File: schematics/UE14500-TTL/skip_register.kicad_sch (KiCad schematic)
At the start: 4 parts, among them U15 74LS02, U16 74LS74

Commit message: Lay out CPU board
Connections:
- net SKIP: now reaches U16.9 (Q)
- no-connect marks 3 -> 2
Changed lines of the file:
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@@
 		(at 177.8 113.03)
 	)
-	(no_connect
-		(at 177.8 72.39)
-	)
 	(wire
 		(pts
@@
 		(pts
 			(xy 142.24 72.39) (xy 162.56 72.39)
+		)
+		(stroke
+			(width 0)
+			(type default)
+		)
+	)
+	(wire
+		(pts
+			(xy 177.8 72.39) (xy 185.42 72.39)
 		)
 		(stroke
@@
 				(hide yes)
 			)
+		)
+	)
+	(global_label "SKIP"
+		(shape output)
+		(at 185.42 72.39 0)
+		(fields_autoplaced yes)
+		(effects
+			(font
+				(size 1.27 1.27)
+			)
+			(justify left)
+		)
+		(property "Intersheetrefs" "${INTERSHEET_REFS}"
+			(at 192.7595 72.39 0)
+			(effects
+				(font
+					(size 1.27 1.27)
+				)
+				(justify left)
+				(hide yes)
+			)

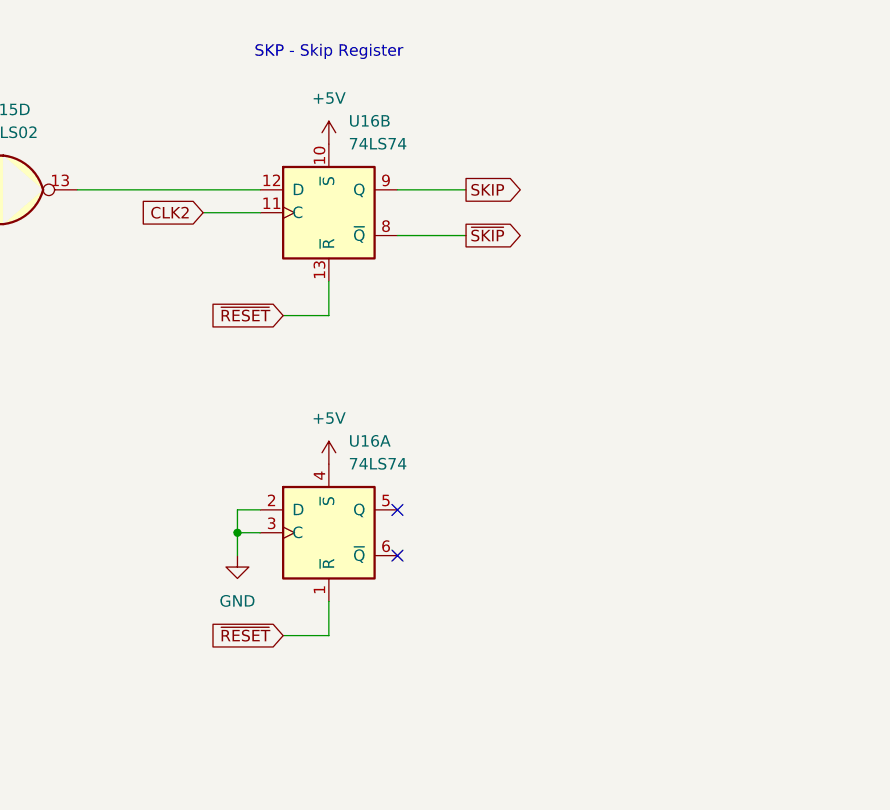
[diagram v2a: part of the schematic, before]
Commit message: Update the CPU schematic with V2 modifications
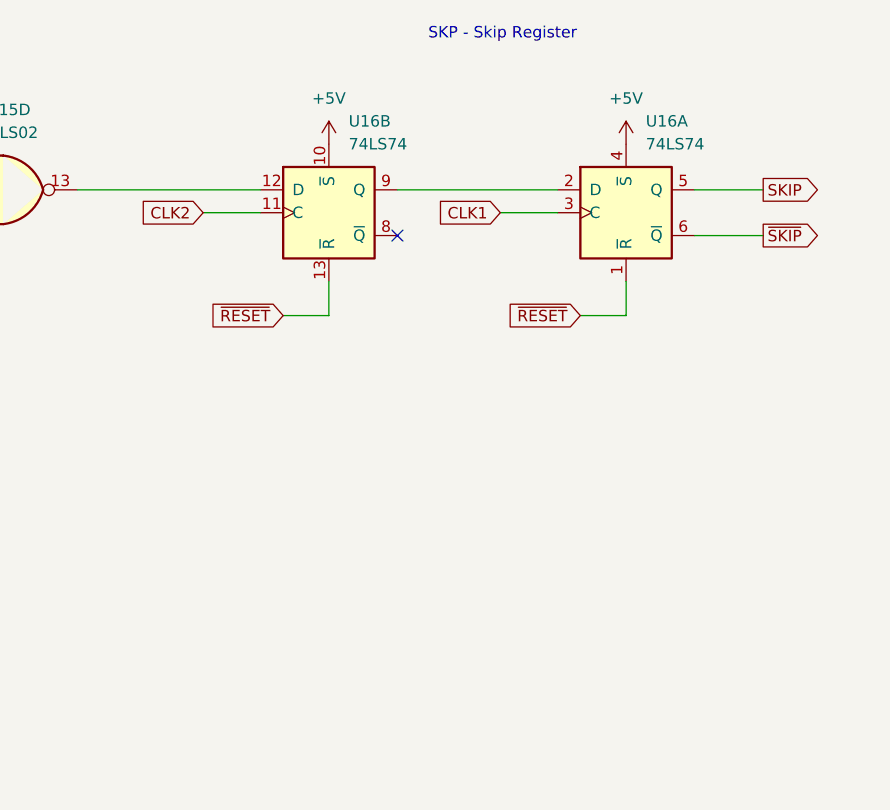
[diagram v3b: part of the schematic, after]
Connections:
- net GND: no longer U16.2 (D), U16.3 (C)
- net SKIP: now also U16.5 (Q); no longer U16.9 (Q)
- net ~{SKIP}: now also U16.6 (~{Q}); no longer U16.8 (~{Q})
- new net: U16.2 (D), U16.9 (Q)
- new net CLK1: U16.3 (C)
- no-connect marks 2 -> 1
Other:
- moved on the sheet: U16A
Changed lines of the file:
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@@
 		(title "UE14500 TTL 1-bit Microprocessor")
 		(date "2025")
-		(rev "1")
+		(rev "2")
 		(comment 1 "Copyright (c) 2025 Rhys Weatherley")
 		(comment 3 "Skip Register")
-	)
-	(junction
-		(at 160.02 110.49)
-		(diameter 0)
-		(color 0 0 0 0)
 	)
 	(junction
@@
 	)
 	(no_connect
-		(at 177.8 107.95)
-	)
-	(no_connect
-		(at 177.8 113.03)
+		(at 177.8 77.47)
 	)
 	(wire
@@
 	(wire
 		(pts
+			(xy 177.8 72.39) (xy 195.58 72.39)
+		)
+		(stroke
+			(width 0)
+			(type default)
+		)
+	)
+	(wire
+		(pts
 			(xy 156.21 74.93) (xy 162.56 74.93)
 		)
@@
 	(wire
 		(pts
-			(xy 177.8 72.39) (xy 185.42 72.39)
+			(xy 210.82 72.39) (xy 218.44 72.39)
 		)
 		(stroke
@@
 	(wire
 		(pts
-			(xy 170.18 121.92) (xy 170.18 118.11)
-		)
-		(stroke
-			(width 0)
-			(type default)
-		)
-	)
-	(wire
-		(pts
-			(xy 165.1 121.92) (xy 170.18 121.92)
+			(xy 203.2 86.36) (xy 203.2 82.55)
+		)
+		(stroke
+			(width 0)
+			(type default)
+		)
+	)
+	(wire
+		(pts
+			(xy 198.12 86.36) (xy 203.2 86.36)
 		)
 		(stroke
@@
 	(wire
 		(pts
-			(xy 160.02 110.49) (xy 160.02 107.95)
-		)
-		(stroke
-			(width 0)
-			(type default)
-		)
-	)
-	(wire
-		(pts
 			(xy 106.68 69.85) (xy 102.87 69.85)
 		)
@@
 	(wire
 		(pts
-			(xy 160.02 107.95) (xy 162.56 107.95)
-		)
-		(stroke
-			(width 0)
-			(type default)
-		)
-	)
-	(wire
-		(pts
 			(xy 80.01 66.04) (xy 80.01 60.96)
 		)
@@
 	(wire
 		(pts
-			(xy 160.02 113.03) (xy 160.02 110.49)
-		)
-		(stroke
-			(width 0)
-			(type default)
-		)
-	)
-	(wire
-		(pts
 			(xy 102.87 74.93) (xy 102.87 81.28)
 		)
@@
 	(wire
 		(pts
-			(xy 160.02 110.49) (xy 162.56 110.49)
-		)
-		(stroke
-			(width 0)
-			(type default)
-		)
-	)
-	(wire
-		(pts
 			(xy 74.93 60.96) (xy 80.01 60.96)
 		)
@@
 	(wire
 		(pts
+			(xy 189.23 74.93) (xy 195.58 74.93)
+		)
+		(stroke
+			(width 0)
+			(type default)
+		)
+	)
+	(wire
+		(pts
 			(xy 102.87 63.5) (xy 97.79 63.5)
 		)
@@
 	(wire
 		(pts
-			(xy 177.8 77.47) (xy 185.42 77.47)
+			(xy 210.82 77.47) (xy 218.44 77.47)
 		)
 		(stroke
@@
 	(text "SKP - Skip Register"
 		(exclude_from_sim no)
-		(at 170.18 57.15 0)
+		(at 189.484 55.118 0)
 		(effects
 			(font
@@
 	(global_label "~{SKIP}"
 		(shape output)
-		(at 185.42 77.47 0)
+		(at 218.44 77.47 0)
 		(fields_autoplaced yes)
 		(effects
@@
 		)
 		(property "Intersheetrefs" "${INTERSHEET_REFS}"
-			(at 192.7595 77.47 0)
+			(at 225.7795 77.47 0)
 			(effects
 				(font
@@
 		)
 	)
-	(global_label "SKIP"
-		(shape output)
-		(at 185.42 72.39 0)
+	(global_label "CLK1"
+		(shape input)
+		(at 189.23 74.93 180)
 		(fields_autoplaced yes)
 		(effects
@@
 				(size 1.27 1.27)
 			)
+			(justify right)
+		)
+		(property "Intersheetrefs" "${INTERSHEET_REFS}"
+			(at 181.4672 74.93 0)
+			(effects
+				(font
+					(size 1.27 1.27)
+				)
+				(justify right)
+				(hide yes)
+			)
+		)
+	)
+	(global_label "SKIP"
+		(shape output)
+		(at 218.44 72.39 0)
+		(fields_autoplaced yes)
+		(effects
+			(font
+				(size 1.27 1.27)
+			)
 			(justify left)
 		)
 		(property "Intersheetrefs" "${INTERSHEET_REFS}"
-			(at 192.7595 72.39 0)
+			(at 225.7795 72.39 0)
 			(effects
 				(font
@@
 	(global_label "~{RESET}"
 		(shape input)
-		(at 165.1 121.92 180)
+		(at 198.12 86.36 180)
 		(fields_autoplaced yes)
 		(effects
@@
 		)
 		(property "Intersheetrefs" "${INTERSHEET_REFS}"
-			(at 156.3697 121.92 0)
+			(at 189.3897 86.36 0)
 			(effects
 				(font
@@
 	(symbol
 		(lib_id "power:+5V")
-		(at 170.18 102.87 0)
+		(at 203.2 67.31 0)
 		(unit 1)
 		(exclude_from_sim no)
@@
 		(fields_autoplaced yes)
 		(property "Reference" "#PWR91"
-			(at 170.18 106.68 0)
+			(at 203.2 71.12 0)
 			(effects
 				(font
@@
 		)
 		(property "Value" "+5V"
-			(at 170.18 97.79 0)
+			(at 203.2 62.23 0)
 			(effects
 				(font
@@
 		)
 		(property "Footprint" ""
-			(at 170.18 102.87 0)
+			(at 203.2 67.31 0)
 			(effects
 				(font
@@
 		)
 		(property "Datasheet" ""
-			(at 170.18 102.87 0)
+			(at 203.2 67.31 0)
 			(effects
 				(font
@@
 		)
 		(property "Description" "Power symbol creates a global label with name \"+5V\""
-			(at 170.18 102.87 0)
+			(at 203.2 67.31 0)
 			(effects
 				(font
@@
 	(symbol
 		(lib_id "74xx:74LS74")
-		(at 170.18 110.49 0)
+		(at 203.2 74.93 0)
 		(unit 1)
 		(exclude_from_sim no)
@@
 		(fields_autoplaced yes)
 		(property "Reference" "U16"
-			(at 172.3741 100.33 0)
+			(at 205.3941 64.77 0)
 			(effects
 				(font
@@
 		)
 		(property "Value" "74LS74"
-			(at 172.3741 102.87 0)
+			(at 205.3941 67.31 0)
 			(effects
 				(font
@@
 		)
 		(property "Footprint" "Package_DIP:DIP-14_W7.62mm"
-			(at 170.18 110.49 0)
+			(at 203.2 74.93 0)
 			(effects
 				(font
@@
 		)
 		(property "Datasheet" "74xx/74hc_hct74.pdf"
-			(at 170.18 110.49 0)
+			(at 203.2 74.93 0)
 			(effects
 				(font
@@
 		)
 		(property "Description" "Dual D Flip-flop, Set & Reset"
-			(at 170.18 110.49 0)
+			(at 203.2 74.93 0)
 			(effects
 				(font
@@
 				)
 			)
-		)
-	)
-	(symbol
-		(lib_id "power:GND")
-		(at 160.02 113.03 0)
-		(unit 1)
-		(exclude_from_sim no)
-		(in_bom yes)
-		(on_board yes)
-		(dnp no)
-		(fields_autoplaced yes)
-		(property "Reference" "#PWR89"
-			(at 160.02 119.38 0)
-			(effects
-				(font
-					(size 1.27 1.27)
-				)
-				(hide yes)
-			)
-		)
-		(property "Value" "GND"
-			(at 160.02 118.11 0)
-			(effects
-				(font
-					(size 1.27 1.27)
-				)
-			)
-		)
-		(property "Footprint" ""
-			(at 160.02 113.03 0)
-			(effects
-				(font
-					(size 1.27 1.27)
-				)
-				(hide yes)
-			)
-		)
-		(property "Datasheet" ""
-			(at 160.02 113.03 0)
-			(effects
-				(font
-					(size 1.27 1.27)
-				)
-				(hide yes)
-			)
-		)
-		(property "Description" "Power symbol creates a global label with name \"GND\" , ground"
-			(at 160.02 113.03 0)
-			(effects
-				(font
-					(size 1.27 1.27)
-				)
-				(hide yes)
-			)
-		)
-		(pin "1"
-		)
-		(instances
-			(project "UE14500-TTL"
-				(path "/3387ba40-0694-43b2-a156-d12ce9552f1f/4d3b60cb-7695-49c7-929a-ce7cab32c354"
-					(reference "#PWR89")
-					(unit 1)
-				)
-			)
